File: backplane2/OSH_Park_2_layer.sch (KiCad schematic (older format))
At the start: 19 parts, among them J1 Conn_02x40_Odd_Even, J10 Conn_01x40, J11 Conn_01x40, J12 Conn_01x40, J13 Conn_01x40, J14 Conn_01x40, J15 Conn_01x40, J16 Conn_01x40, J17 Conn_01x40, J18 Conn_01x40, J19 Conn_01x40, J2 Conn_02x40_Odd_Even, J20 Conn_01x02, J21 OSTTA020161, J3 Conn_02x40_Odd_Even, J4 Conn_02x40_Odd_Even, J5 Conn_02x40_Odd_Even, J6 Conn_02x40_Odd_Even, J7 Conn_02x40_Odd_Even

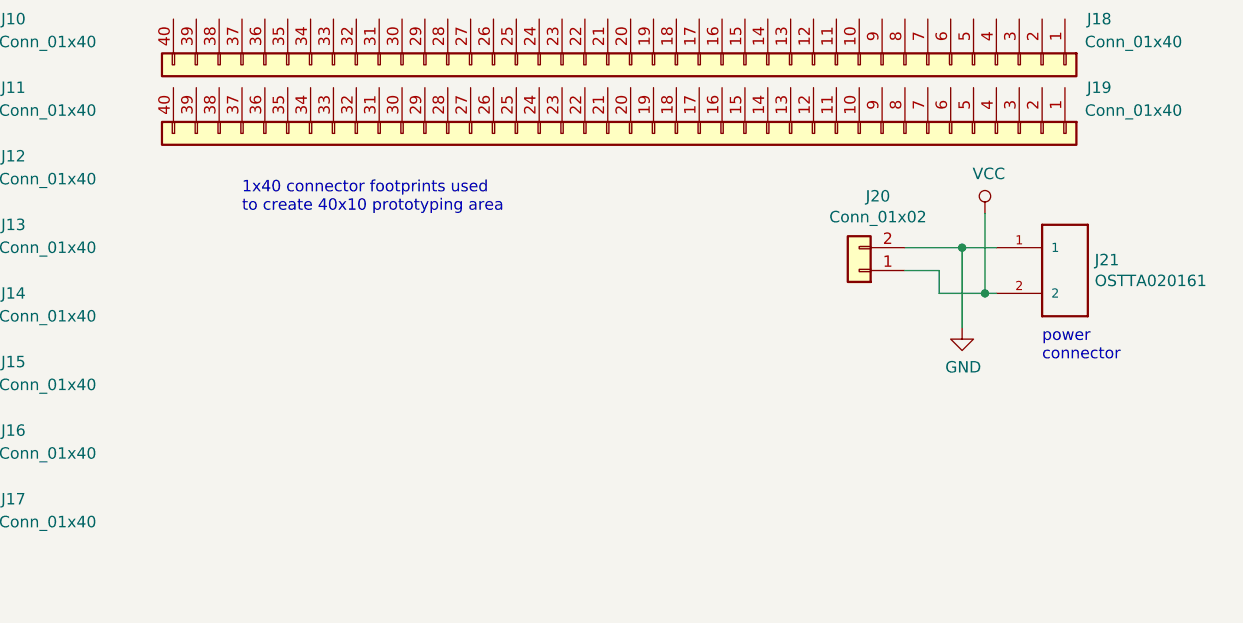
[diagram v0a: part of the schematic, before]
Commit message: added power connector and power LED
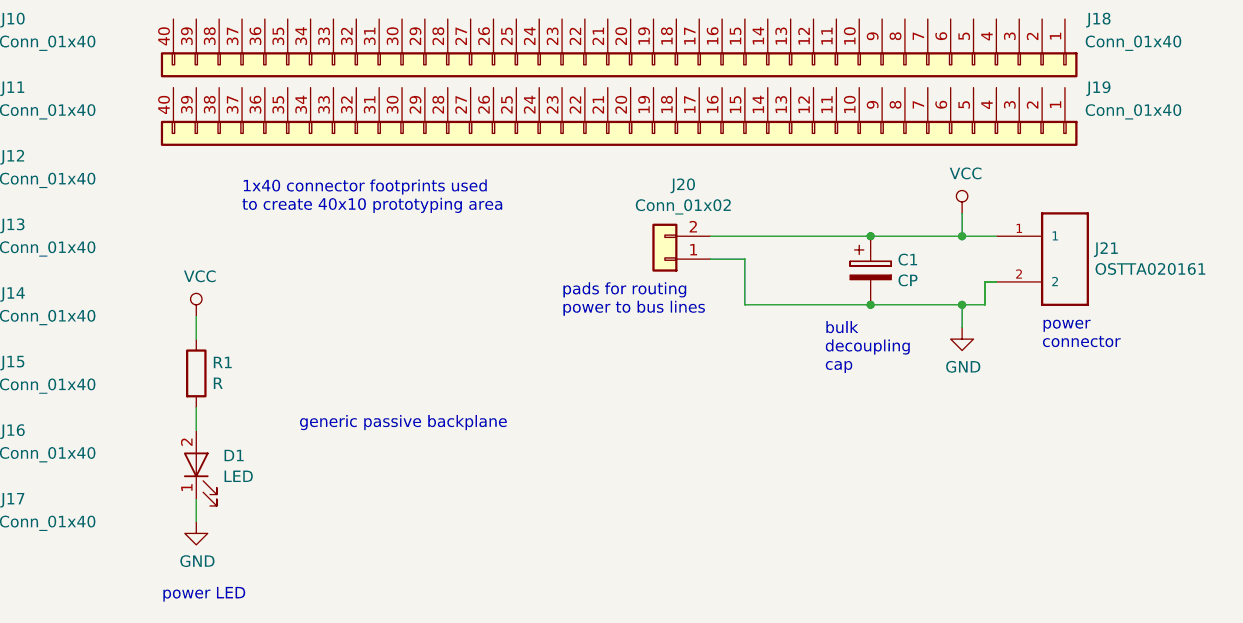
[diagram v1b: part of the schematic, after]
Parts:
- added C1: CP, symbol device:CP
- added D1: LED, symbol device:LED
- added R1: R, symbol device:R
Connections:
- wire segments 568 -> 575
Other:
- note added: "bulk\ndecoupling\ncap"
- note added: "generic passive backplane"
- note added: "pads for routing\npower to bus lines"
- note added: "power LED"
- moved on the sheet: J20, J21
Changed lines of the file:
@@
 L power:VCC #PWR?
 U 1 1 5EBA37E3
-P 9350 6000
-F 0 "#PWR?" H 9350 5850 50  0001 C CNN
-F 1 "VCC" H 9367 6173 50  0000 C CNN
-F 2 "" H 9350 6000 50  0001 C CNN
-F 3 "" H 9350 6000 50  0001 C CNN
-	1    9350 6000
+P 9250 6000
+F 0 "#PWR?" H 9250 5850 50  0001 C CNN
+F 1 "VCC" H 9267 6173 50  0000 C CNN
+F 2 "" H 9250 6000 50  0001 C CNN
+F 3 "" H 9250 6000 50  0001 C CNN
+	1    9250 6000
 	1    0    0    -1
 $EndComp
 Wire Wire Line
-	9400 6350 9350 6350
-Wire Wire Line
-	9400 6150 9250 6150
+	9400 6300 9350 6300
 $Comp
 L power:GND #PWR?
@@
 L OSTTA020161:OSTTA020161 J21
 U 1 1 5EAB2FAF
-P 9700 6250
-F 0 "J21" H 9830 6296 50  0000 L CNN
-F 1 "OSTTA020161" H 9830 6205 50  0000 L CNN
-F 2 "OST_OSTTA020161" H 9700 6250 50  0001 L BNN
-F 3 "Connector Terminal Blocks 2 Position 5mm Solder Straight Thru-Hole 16A" H 9700 6250 50  0001 L BNN
-F 4 "Unavailable" H 9700 6250 50  0001 L BNN "Field4"
-F 5 "On Shore" H 9700 6250 50  0001 L BNN "Field5"
-F 6 "None" H 9700 6250 50  0001 L BNN "Field6"
-F 7 "None" H 9700 6250 50  0001 L BNN "Field7"
-F 8 "OSTTA020161" H 9700 6250 50  0001 L BNN "Field8"
-	1    9700 6250
+P 9700 6200
+F 0 "J21" H 9830 6246 50  0000 L CNN
+F 1 "OSTTA020161" H 9830 6155 50  0000 L CNN
+F 2 "OST_OSTTA020161" H 9700 6200 50  0001 L BNN
+F 3 "Connector Terminal Blocks 2 Position 5mm Solder Straight Thru-Hole 16A" H 9700 6200 50  0001 L BNN
+F 4 "Unavailable" H 9700 6200 50  0001 L BNN "Field4"
+F 5 "On Shore" H 9700 6200 50  0001 L BNN "Field5"
+F 6 "None" H 9700 6200 50  0001 L BNN "Field6"
+F 7 "None" H 9700 6200 50  0001 L BNN "Field7"
+F 8 "OSTTA020161" H 9700 6200 50  0001 L BNN "Field8"
+	1    9700 6200
+	1    0    0    -1
+$EndComp
+$Comp
+L Connector_Generic:Conn_01x02 J20
+U 1 1 5EEE3B00
+P 7950 6200
+F 0 "J20" H 7868 5875 50  0000 C CNN
+F 1 "Conn_01x02" H 7868 5966 50  0000 C CNN
+F 2 "" H 7950 6200 50  0001 C CNN
+F 3 "~" H 7950 6200 50  0001 C CNN
+	1    7950 6200
+	-1   0    0    1
+$EndComp
+Wire Wire Line
+	8300 6200 8150 6200
+Text Notes 9600 6600 0    50   ~ 0
+power\nconnector
+Text Notes 6350 6950 0    50   ~ 0
+generic passive backplane
+$Comp
+L device:CP C1
+U 1 1 5F262008
+P 8850 6250
+F 0 "C1" H 8968 6296 50  0000 L CNN
+F 1 "CP" H 8968 6205 50  0000 L CNN
+F 2 "" H 8888 6100 50  0001 C CNN
+F 3 "" H 8850 6250 50  0001 C CNN
+	1    8850 6250
 	1    0    0    -1
 $EndComp
 Wire Wire Line
-	9250 6500 9250 6150
-Connection ~ 9250 6150
+	8150 6100 8850 6100
+Connection ~ 8850 6100
 Wire Wire Line
-	9350 6000 9350 6350
-Connection ~ 9350 6350
+	8850 6100 9250 6100
 Wire Wire Line
-	9350 6350 9150 6350
+	9350 6300 9350 6400
+Wire Wire Line
+	9350 6400 9250 6400
+Wire Wire Line
+	8300 6400 8850 6400
+Wire Wire Line
+	8300 6200 8300 6400
+Connection ~ 8850 6400
+Wire Wire Line
+	9250 6500 9250 6400
+Connection ~ 9250 6400
+Wire Wire Line
+	9250 6400 8850 6400
+Wire Wire Line
+	9250 6000 9250 6100
+Connection ~ 9250 6100
+Wire Wire Line
+	9250 6100 9400 6100
+Text Notes 7500 6450 0    50   ~ 0
+pads for routing\npower to bus lines
 $Comp
-L Connector_Generic:Conn_01x02 J20
-U 1 1 5EEE3B00
-P 8800 6250
-F 0 "J20" H 8718 5925 50  0000 C CNN
-F 1 "Conn_01x02" H 8718 6016 50  0000 C CNN
-F 2 "" H 8800 6250 50  0001 C CNN
-F 3 "~" H 8800 6250 50  0001 C CNN
-	1    8800 6250
-	-1   0    0    1
+L device:R R1
+U 1 1 5F59CCFE
+P 5900 6700
+F 0 "R1" H 5970 6746 50  0000 L CNN
+F 1 "R" H 5970 6655 50  0000 L CNN
+F 2 "" V 5830 6700 50  0001 C CNN
+F 3 "" H 5900 6700 50  0001 C CNN
+	1    5900 6700
+	1    0    0    -1
+$EndComp
+$Comp
+L device:LED D1
+U 1 1 5F59F20B
+P 5900 7100
+F 0 "D1" V 5939 6983 50  0000 R CNN
+F 1 "LED" V 5848 6983 50  0000 R CNN
+F 2 "" H 5900 7100 50  0001 C CNN
+F 3 "" H 5900 7100 50  0001 C CNN
+	1    5900 7100
+	0    -1   -1   0
 $EndComp
 Wire Wire Line
-	9250 6150 9000 6150
+	5900 6950 5900 6850
 Wire Wire Line
-	9150 6350 9150 6250
+	5900 6550 5900 6450
+$Comp
+L power:VCC #PWR?
+U 1 1 5F888505
+P 5900 6450
+F 0 "#PWR?" H 5900 6300 50  0001 C CNN
+F 1 "VCC" H 5917 6623 50  0000 C CNN
+F 2 "" H 5900 6450 50  0001 C CNN
+F 3 "" H 5900 6450 50  0001 C CNN
+	1    5900 6450
+	1    0    0    -1
+$EndComp
 Wire Wire Line
-	9150 6250 9000 6250
-Text Notes 9600 6650 0    50   ~ 0
-power\nconnector
+	5900 7250 5900 7350
+$Comp
+L power:GND #PWR?
+U 1 1 5F902501
+P 5900 7350
+F 0 "#PWR?" H 5900 7100 50  0001 C CNN
+F 1 "GND" H 5905 7177 50  0000 C CNN
+F 2 "" H 5900 7350 50  0001 C CNN
+F 3 "" H 5900 7350 50  0001 C CNN
+	1    5900 7350
+	1    0    0    -1
+$EndComp
+Text Notes 8650 6700 0    50   ~ 0
+bulk\ndecoupling\ncap
+Text Notes 5750 7700 0    50   ~ 0
+power LED
 $EndSCHEMATC

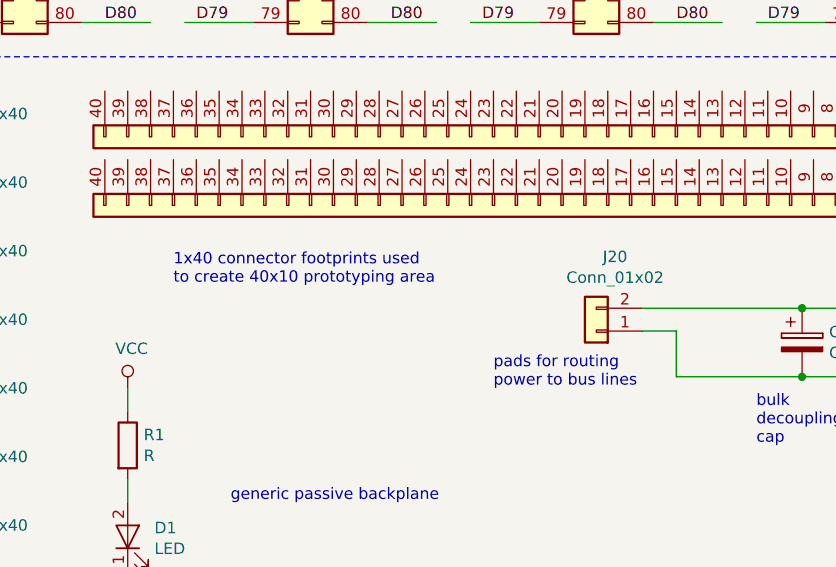
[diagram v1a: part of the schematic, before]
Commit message: selected component footprints
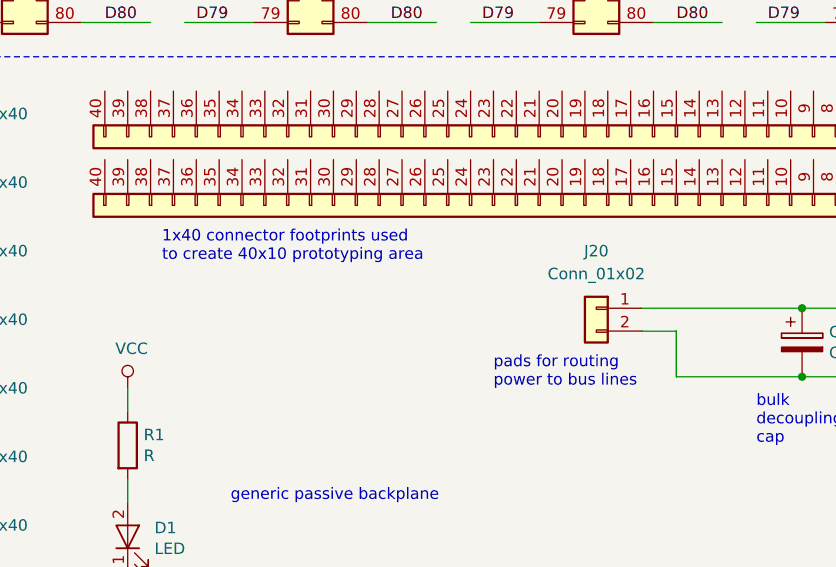
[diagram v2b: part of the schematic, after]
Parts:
- C1: footprint (none) -> Capacitor_THT:CP_Radial_D10.0mm_P5.00mm
- D1: footprint (none) -> LED_THT:LED_D5.0mm
- J1, J2, J3, J4, J5, J6, J7: footprint (none) -> Connector_PinSocket_2.54mm:PinSocket_2x40_P2.54mm_Vertical
- J10, J11, J12, J13, J14, J15, J16, J17, J18, J19, J20: footprint (none) -> Connector_PinSocket_2.54mm:PinSocket_1x40_P2.54mm_Vertical
- J21: footprint OST_OSTTA020161 -> OSTTA020161:OST_OSTTA020161
- R1: footprint (none) -> Resistor_THT:R_Axial_DIN0204_L3.6mm_D1.6mm_P7.62mm_Horizontal
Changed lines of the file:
@@
 F 0 "J1" H 1700 4967 50  0000 C CNN
 F 1 "Conn_02x40_Odd_Even" H 1700 4876 50  0000 C CNN
-F 2 "" H 1650 2850 50  0001 C CNN
+F 2 "Connector_PinSocket_2.54mm:PinSocket_2x40_P2.54mm_Vertical" H 1650 2850 50  0001 C CNN
 F 3 "~" H 1650 2850 50  0001 C CNN
 	1    1650 2850
@@
 F 0 "J2" H 2950 4967 50  0000 C CNN
 F 1 "Conn_02x40_Odd_Even" H 2950 4876 50  0000 C CNN
-F 2 "" H 2900 2850 50  0001 C CNN
+F 2 "Connector_PinSocket_2.54mm:PinSocket_2x40_P2.54mm_Vertical" H 2900 2850 50  0001 C CNN
 F 3 "~" H 2900 2850 50  0001 C CNN
 	1    2900 2850
@@
 F 0 "J3" H 4200 4967 50  0000 C CNN
 F 1 "Conn_02x40_Odd_Even" H 4200 4876 50  0000 C CNN
-F 2 "" H 4150 2850 50  0001 C CNN
+F 2 "Connector_PinSocket_2.54mm:PinSocket_2x40_P2.54mm_Vertical" H 4150 2850 50  0001 C CNN
 F 3 "~" H 4150 2850 50  0001 C CNN
 	1    4150 2850
@@
 F 0 "J4" H 5450 4967 50  0000 C CNN
 F 1 "Conn_02x40_Odd_Even" H 5450 4876 50  0000 C CNN
-F 2 "" H 5400 2850 50  0001 C CNN
+F 2 "Connector_PinSocket_2.54mm:PinSocket_2x40_P2.54mm_Vertical" H 5400 2850 50  0001 C CNN
 F 3 "~" H 5400 2850 50  0001 C CNN
 	1    5400 2850
@@
 F 0 "J5" H 6700 4967 50  0000 C CNN
 F 1 "Conn_02x40_Odd_Even" H 6700 4876 50  0000 C CNN
-F 2 "" H 6650 2850 50  0001 C CNN
+F 2 "Connector_PinSocket_2.54mm:PinSocket_2x40_P2.54mm_Vertical" H 6650 2850 50  0001 C CNN
 F 3 "~" H 6650 2850 50  0001 C CNN
 	1    6650 2850
@@
 F 0 "J6" H 7950 4967 50  0000 C CNN
 F 1 "Conn_02x40_Odd_Even" H 7950 4876 50  0000 C CNN
-F 2 "" H 7900 2850 50  0001 C CNN
+F 2 "Connector_PinSocket_2.54mm:PinSocket_2x40_P2.54mm_Vertical" H 7900 2850 50  0001 C CNN
 F 3 "~" H 7900 2850 50  0001 C CNN
 	1    7900 2850
@@
 F 0 "J7" H 9200 4967 50  0000 C CNN
 F 1 "Conn_02x40_Odd_Even" H 9200 4876 50  0000 C CNN
-F 2 "" H 9150 2850 50  0001 C CNN
+F 2 "Connector_PinSocket_2.54mm:PinSocket_2x40_P2.54mm_Vertical" H 9150 2850 50  0001 C CNN
 F 3 "~" H 9150 2850 50  0001 C CNN
 	1    9150 2850
@@
 F 0 "J10" V 2850 7400 50  0000 C CNN
 F 1 "Conn_01x40" V 2950 7550 50  0000 C CNN
-F 2 "" H 3050 5350 50  0001 C CNN
+F 2 "Connector_PinSocket_2.54mm:PinSocket_1x40_P2.54mm_Vertical" H 3050 5350 50  0001 C CNN
 F 3 "~" H 3050 5350 50  0001 C CNN
 	1    3050 5350
@@
 F 0 "J11" V 2850 7700 50  0000 C CNN
 F 1 "Conn_01x40" V 2950 7850 50  0000 C CNN
-F 2 "" H 3050 5650 50  0001 C CNN
+F 2 "Connector_PinSocket_2.54mm:PinSocket_1x40_P2.54mm_Vertical" H 3050 5650 50  0001 C CNN
 F 3 "~" H 3050 5650 50  0001 C CNN
 	1    3050 5650
@@
 F 0 "J12" V 2850 8000 50  0000 C CNN
 F 1 "Conn_01x40" V 2950 8150 50  0000 C CNN
-F 2 "" H 3050 5950 50  0001 C CNN
+F 2 "Connector_PinSocket_2.54mm:PinSocket_1x40_P2.54mm_Vertical" H 3050 5950 50  0001 C CNN
 F 3 "~" H 3050 5950 50  0001 C CNN
 	1    3050 5950
@@
 F 0 "J13" V 2850 8300 50  0000 C CNN
 F 1 "Conn_01x40" V 2950 8450 50  0000 C CNN
-F 2 "" H 3050 6250 50  0001 C CNN
+F 2 "Connector_PinSocket_2.54mm:PinSocket_1x40_P2.54mm_Vertical" H 3050 6250 50  0001 C CNN
 F 3 "~" H 3050 6250 50  0001 C CNN
 	1    3050 6250
@@
 F 0 "J14" V 2850 8600 50  0000 C CNN
 F 1 "Conn_01x40" V 2950 8750 50  0000 C CNN
-F 2 "" H 3050 6550 50  0001 C CNN
+F 2 "Connector_PinSocket_2.54mm:PinSocket_1x40_P2.54mm_Vertical" H 3050 6550 50  0001 C CNN
 F 3 "~" H 3050 6550 50  0001 C CNN
 	1    3050 6550
@@
 F 0 "J15" V 2850 8900 50  0000 C CNN
 F 1 "Conn_01x40" V 2950 9050 50  0000 C CNN
-F 2 "" H 3050 6850 50  0001 C CNN
+F 2 "Connector_PinSocket_2.54mm:PinSocket_1x40_P2.54mm_Vertical" H 3050 6850 50  0001 C CNN
 F 3 "~" H 3050 6850 50  0001 C CNN
 	1    3050 6850
@@
 F 0 "J16" V 2850 9200 50  0000 C CNN
 F 1 "Conn_01x40" V 2950 9350 50  0000 C CNN
-F 2 "" H 3050 7150 50  0001 C CNN
+F 2 "Connector_PinSocket_2.54mm:PinSocket_1x40_P2.54mm_Vertical" H 3050 7150 50  0001 C CNN
 F 3 "~" H 3050 7150 50  0001 C CNN
 	1    3050 7150
@@
 F 0 "J17" V 2850 9500 50  0000 C CNN
 F 1 "Conn_01x40" V 2950 9650 50  0000 C CNN
-F 2 "" H 3050 7450 50  0001 C CNN
+F 2 "Connector_PinSocket_2.54mm:PinSocket_1x40_P2.54mm_Vertical" H 3050 7450 50  0001 C CNN
 F 3 "~" H 3050 7450 50  0001 C CNN
 	1    3050 7450
@@
 F 0 "J18" V 7600 7400 50  0000 C CNN
 F 1 "Conn_01x40" V 7700 7550 50  0000 C CNN
-F 2 "" H 7800 5350 50  0001 C CNN
+F 2 "Connector_PinSocket_2.54mm:PinSocket_1x40_P2.54mm_Vertical" H 7800 5350 50  0001 C CNN
 F 3 "~" H 7800 5350 50  0001 C CNN
 	1    7800 5350
@@
 F 0 "J19" V 7600 7700 50  0000 C CNN
 F 1 "Conn_01x40" V 7700 7850 50  0000 C CNN
-F 2 "" H 7800 5650 50  0001 C CNN
+F 2 "Connector_PinSocket_2.54mm:PinSocket_1x40_P2.54mm_Vertical" H 7800 5650 50  0001 C CNN
 F 3 "~" H 7800 5650 50  0001 C CNN
 	1    7800 5650
 	0    1    1    0
 $EndComp
-Text Notes 6100 6000 0    50   ~ 0
+Text Notes 6050 5900 0    50   ~ 0
 1x40 connector footprints used\nto create 40x10 prototyping area
 $Comp
-L power:VCC #PWR?
+L power:VCC #PWR0101
 U 1 1 5EBA37E3
 P 9250 6000
-F 0 "#PWR?" H 9250 5850 50  0001 C CNN
+F 0 "#PWR0101" H 9250 5850 50  0001 C CNN
 F 1 "VCC" H 9267 6173 50  0000 C CNN
 F 2 "" H 9250 6000 50  0001 C CNN
@@
 	9400 6300 9350 6300
 $Comp
-L power:GND #PWR?
+L power:GND #PWR0102
 U 1 1 5EC1AA77
 P 9250 6500
-F 0 "#PWR?" H 9250 6250 50  0001 C CNN
+F 0 "#PWR0102" H 9250 6250 50  0001 C CNN
 F 1 "GND" H 9255 6327 50  0000 C CNN
 F 2 "" H 9250 6500 50  0001 C CNN
@@
 F 0 "J21" H 9830 6246 50  0000 L CNN
 F 1 "OSTTA020161" H 9830 6155 50  0000 L CNN
-F 2 "OST_OSTTA020161" H 9700 6200 50  0001 L BNN
+F 2 "OSTTA020161:OST_OSTTA020161" H 9700 6200 50  0001 L BNN
 F 3 "Connector Terminal Blocks 2 Position 5mm Solder Straight Thru-Hole 16A" H 9700 6200 50  0001 L BNN
 F 4 "Unavailable" H 9700 6200 50  0001 L BNN "Field4"
@@
 L Connector_Generic:Conn_01x02 J20
 U 1 1 5EEE3B00
-P 7950 6200
-F 0 "J20" H 7868 5875 50  0000 C CNN
-F 1 "Conn_01x02" H 7868 5966 50  0000 C CNN
-F 2 "" H 7950 6200 50  0001 C CNN
-F 3 "~" H 7950 6200 50  0001 C CNN
-	1    7950 6200
-	-1   0    0    1
+P 7950 6100
+F 0 "J20" H 7950 6350 50  0000 C CNN
+F 1 "Conn_01x02" H 7950 6250 50  0000 C CNN
+F 2 "Connector_PinSocket_2.54mm:PinSocket_1x40_P2.54mm_Vertical" H 7950 6100 50  0001 C CNN
+F 3 "~" H 7950 6100 50  0001 C CNN
+	1    7950 6100
+	-1   0    0    -1
 $EndComp
-Wire Wire Line
-	8300 6200 8150 6200
 Text Notes 9600 6600 0    50   ~ 0
 power\nconnector
@@
 F 0 "C1" H 8968 6296 50  0000 L CNN
 F 1 "CP" H 8968 6205 50  0000 L CNN
-F 2 "" H 8888 6100 50  0001 C CNN
+F 2 "Capacitor_THT:CP_Radial_D10.0mm_P5.00mm" H 8888 6100 50  0001 C CNN
 F 3 "" H 8850 6250 50  0001 C CNN
 	1    8850 6250
@@
 F 0 "R1" H 5970 6746 50  0000 L CNN
 F 1 "R" H 5970 6655 50  0000 L CNN
-F 2 "" V 5830 6700 50  0001 C CNN
+F 2 "Resistor_THT:R_Axial_DIN0204_L3.6mm_D1.6mm_P7.62mm_Horizontal" V 5830 6700 50  0001 C CNN
 F 3 "" H 5900 6700 50  0001 C CNN
 	1    5900 6700
@@
 F 0 "D1" V 5939 6983 50  0000 R CNN
 F 1 "LED" V 5848 6983 50  0000 R CNN
-F 2 "" H 5900 7100 50  0001 C CNN
+F 2 "LED_THT:LED_D5.0mm" H 5900 7100 50  0001 C CNN
 F 3 "" H 5900 7100 50  0001 C CNN
 	1    5900 7100
@@
 	5900 6550 5900 6450
 $Comp
-L power:VCC #PWR?
+L power:VCC #PWR0103
 U 1 1 5F888505
 P 5900 6450
-F 0 "#PWR?" H 5900 6300 50  0001 C CNN
+F 0 "#PWR0103" H 5900 6300 50  0001 C CNN
 F 1 "VCC" H 5917 6623 50  0000 C CNN
 F 2 "" H 5900 6450 50  0001 C CNN
@@
 	5900 7250 5900 7350
 $Comp
-L power:GND #PWR?
+L power:GND #PWR0104
 U 1 1 5F902501
 P 5900 7350
-F 0 "#PWR?" H 5900 7100 50  0001 C CNN
+F 0 "#PWR0104" H 5900 7100 50  0001 C CNN
 F 1 "GND" H 5905 7177 50  0000 C CNN
 F 2 "" H 5900 7350 50  0001 C CNN
@@
 Text Notes 5750 7700 0    50   ~ 0
 power LED
+Wire Wire Line
+	8300 6200 8150 6200
 $EndSCHEMATC
